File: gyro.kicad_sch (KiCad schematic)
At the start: 6 parts, among them U4 I3G4250D

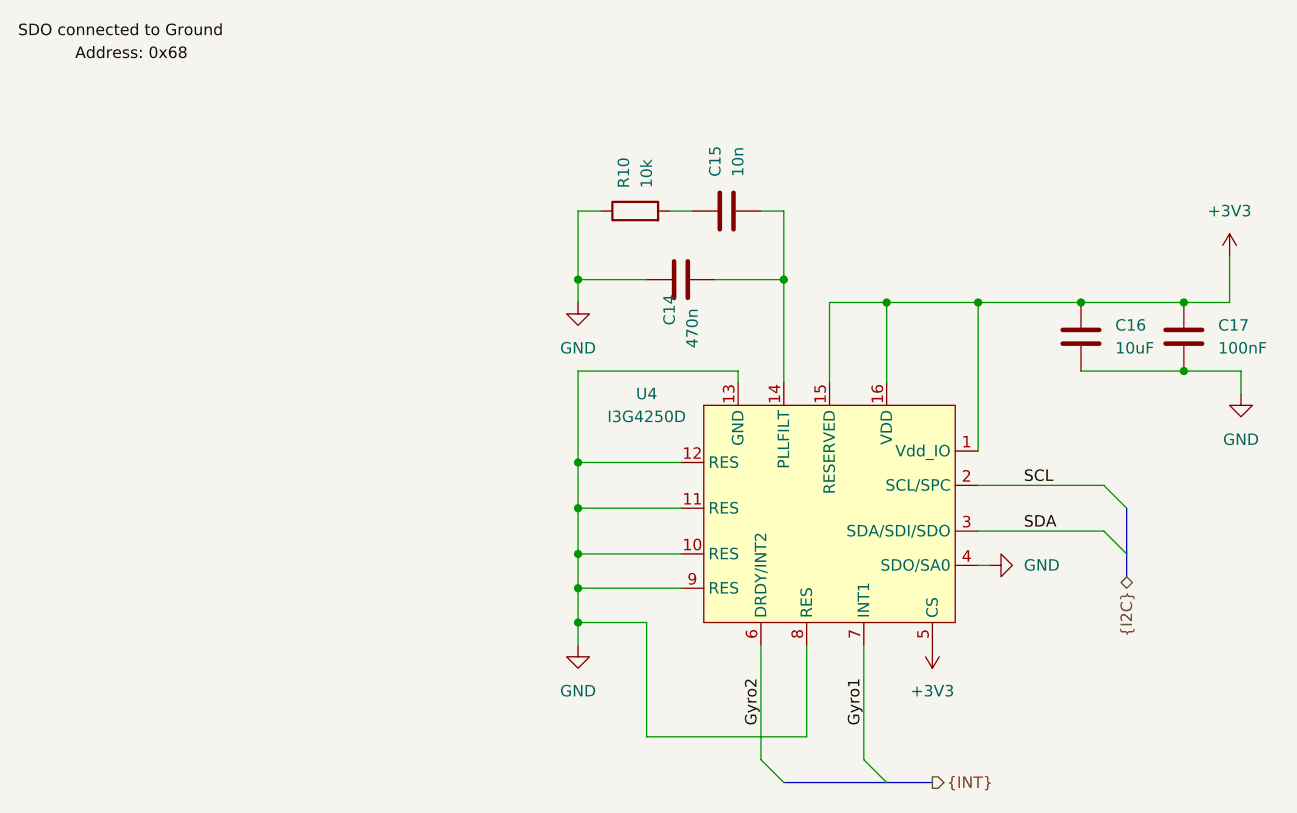
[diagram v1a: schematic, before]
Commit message: Geographical reannotated
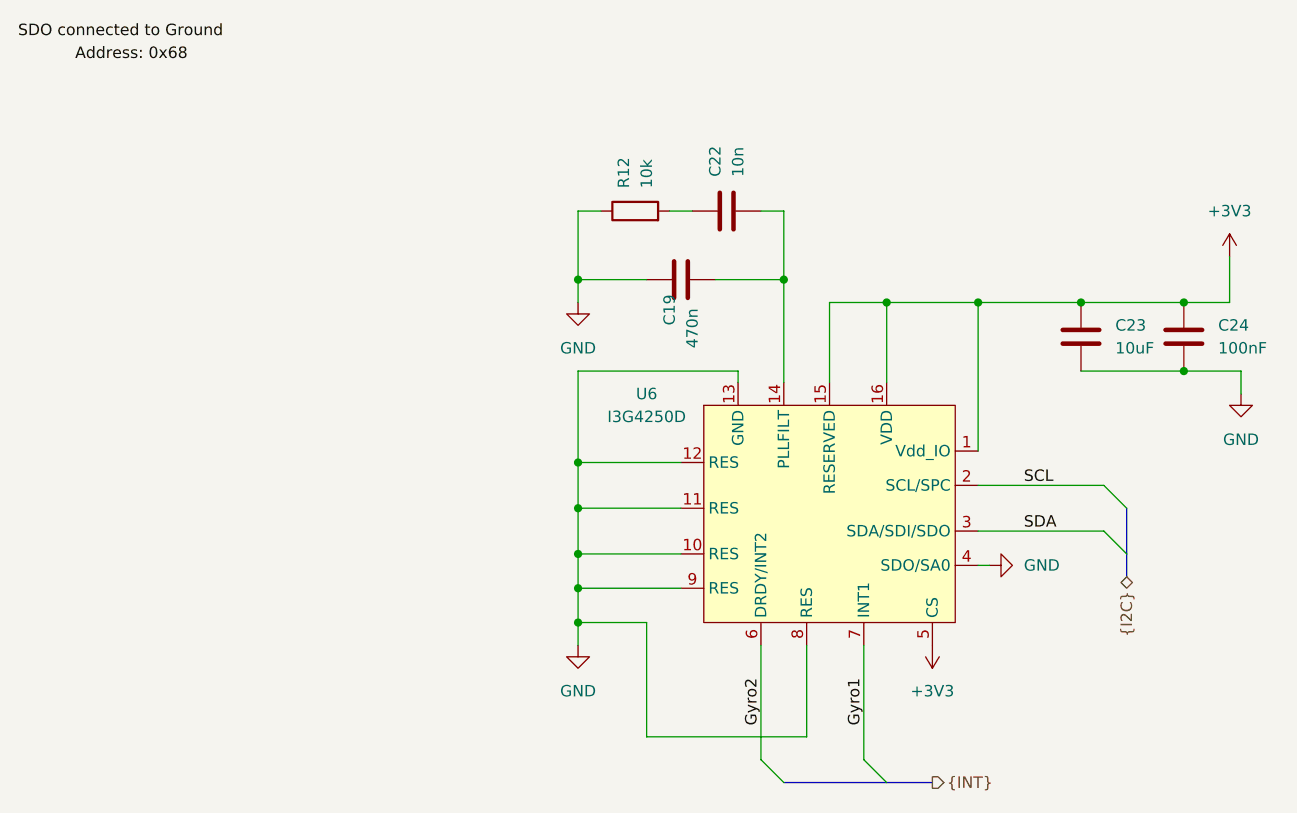
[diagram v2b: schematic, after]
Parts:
- renumbered C14 to C19, C15 to C22, C16 to C23, C17 to C24, R10 to R12, U4 to U6
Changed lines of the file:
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@@
   (symbol (lib_id "Device:C") (at 143.51 49.53 0) (unit 1)
     (in_bom yes) (on_board yes)
-    (property "Reference" "C17" (id 0) (at 147.32 48.26 0)
+    (property "Reference" "C24" (id 0) (at 147.32 48.26 0)
       (effects (font (size 1.27 1.27)) (justify left))
     )
@@
   (symbol (lib_id "Device:C") (at 132.08 49.53 0) (unit 1)
     (in_bom yes) (on_board yes)
-    (property "Reference" "C16" (id 0) (at 135.89 48.26 0)
+    (property "Reference" "C23" (id 0) (at 135.89 48.26 0)
       (effects (font (size 1.27 1.27)) (justify left))
     )
@@
   (symbol (lib_id "Device:C") (at 87.63 43.18 90) (mirror x) (unit 1)
     (in_bom yes) (on_board yes)
-    (property "Reference" "C14" (id 0) (at 86.36 48.26 0)
+    (property "Reference" "C19" (id 0) (at 86.36 48.26 0)
       (effects (font (size 1.27 1.27)) (justify right))
     )
@@
   (symbol (lib_id "Device:C") (at 92.71 35.56 270) (unit 1)
     (in_bom yes) (on_board yes) (fields_autoplaced)
-    (property "Reference" "C15" (id 0) (at 91.4399 31.75 0)
+    (property "Reference" "C22" (id 0) (at 91.4399 31.75 0)
       (effects (font (size 1.27 1.27)) (justify right))
     )
@@
   (symbol (lib_id "Device:R") (at 82.55 35.56 90) (unit 1)
     (in_bom yes) (on_board yes) (fields_autoplaced)
-    (property "Reference" "R10" (id 0) (at 81.2799 33.02 0)
+    (property "Reference" "R12" (id 0) (at 81.2799 33.02 0)
       (effects (font (size 1.27 1.27)) (justify left))
     )
@@
   (symbol (lib_id "Sensor:I3G4250D") (at 97.79 46.99 0) (unit 1)
     (in_bom yes) (on_board yes)
-    (property "Reference" "U4" (id 0) (at 83.82 55.88 0))
+    (property "Reference" "U6" (id 0) (at 83.82 55.88 0))
     (property "Value" "I3G4250D" (id 1) (at 83.82 58.42 0))
     (property "Footprint" "YAR_Sensors:I3G4250D" (id 2) (at 97.79 46.99 0)

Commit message: Final refinements before issue to JLC
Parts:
- renumbered C19 to C14, C22 to C15, C23 to C16, C24 to C17, R12 to R10, U6 to U4
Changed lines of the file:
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@@
   (symbol (lib_id "power:GND") (at 76.2 83.82 0) (unit 1)
     (in_bom yes) (on_board yes) (fields_autoplaced)
-    (property "Reference" "#PWR031" (id 0) (at 76.2 90.17 0)
+    (property "Reference" "#PWR033" (id 0) (at 76.2 90.17 0)
       (effects (font (size 1.27 1.27)) hide)
     )
@@
   (symbol (lib_id "Device:C") (at 143.51 49.53 0) (unit 1)
     (in_bom yes) (on_board yes)
-    (property "Reference" "C24" (id 0) (at 147.32 48.26 0)
+    (property "Reference" "C17" (id 0) (at 147.32 48.26 0)
       (effects (font (size 1.27 1.27)) (justify left))
     )
@@
   (symbol (lib_id "power:GND") (at 76.2 45.72 0) (unit 1)
     (in_bom yes) (on_board yes) (fields_autoplaced)
-    (property "Reference" "#PWR030" (id 0) (at 76.2 52.07 0)
+    (property "Reference" "#PWR032" (id 0) (at 76.2 52.07 0)
       (effects (font (size 1.27 1.27)) hide)
     )
@@
   (symbol (lib_id "Device:C") (at 132.08 49.53 0) (unit 1)
     (in_bom yes) (on_board yes)
-    (property "Reference" "C23" (id 0) (at 135.89 48.26 0)
+    (property "Reference" "C16" (id 0) (at 135.89 48.26 0)
       (effects (font (size 1.27 1.27)) (justify left))
     )
@@
   (symbol (lib_id "power:+3V3") (at 115.57 83.82 180) (unit 1)
     (in_bom yes) (on_board yes) (fields_autoplaced)
-    (property "Reference" "#PWR032" (id 0) (at 115.57 80.01 0)
+    (property "Reference" "#PWR034" (id 0) (at 115.57 80.01 0)
       (effects (font (size 1.27 1.27)) hide)
     )
@@
   (symbol (lib_id "power:+3V3") (at 148.59 40.64 0) (unit 1)
     (in_bom yes) (on_board yes) (fields_autoplaced)
-    (property "Reference" "#PWR034" (id 0) (at 148.59 44.45 0)
+    (property "Reference" "#PWR036" (id 0) (at 148.59 44.45 0)
       (effects (font (size 1.27 1.27)) hide)
     )
@@
   (symbol (lib_id "Device:C") (at 87.63 43.18 90) (mirror x) (unit 1)
     (in_bom yes) (on_board yes)
-    (property "Reference" "C19" (id 0) (at 86.36 48.26 0)
+    (property "Reference" "C14" (id 0) (at 86.36 48.26 0)
       (effects (font (size 1.27 1.27)) (justify right))
     )
@@
   (symbol (lib_id "power:GND") (at 149.86 55.88 0) (unit 1)
     (in_bom yes) (on_board yes) (fields_autoplaced)
-    (property "Reference" "#PWR035" (id 0) (at 149.86 62.23 0)
+    (property "Reference" "#PWR037" (id 0) (at 149.86 62.23 0)
       (effects (font (size 1.27 1.27)) hide)
     )
@@
   (symbol (lib_id "Device:C") (at 92.71 35.56 270) (unit 1)
     (in_bom yes) (on_board yes) (fields_autoplaced)
-    (property "Reference" "C22" (id 0) (at 91.4399 31.75 0)
+    (property "Reference" "C15" (id 0) (at 91.4399 31.75 0)
       (effects (font (size 1.27 1.27)) (justify right))
     )
@@
   (symbol (lib_id "Device:R") (at 82.55 35.56 90) (unit 1)
     (in_bom yes) (on_board yes) (fields_autoplaced)
-    (property "Reference" "R12" (id 0) (at 81.2799 33.02 0)
+    (property "Reference" "R10" (id 0) (at 81.2799 33.02 0)
       (effects (font (size 1.27 1.27)) (justify left))
     )
@@
   (symbol (lib_id "Sensor:I3G4250D") (at 97.79 46.99 0) (unit 1)
     (in_bom yes) (on_board yes)
-    (property "Reference" "U6" (id 0) (at 83.82 55.88 0))
+    (property "Reference" "U4" (id 0) (at 83.82 55.88 0))
     (property "Value" "I3G4250D" (id 1) (at 83.82 58.42 0))
     (property "Footprint" "YAR_Sensors:I3G4250D" (id 2) (at 97.79 46.99 0)
@@
   (symbol (lib_id "power:GND") (at 121.92 74.93 90) (unit 1)
     (in_bom yes) (on_board yes) (fields_autoplaced)
-    (property "Reference" "#PWR033" (id 0) (at 128.27 74.93 0)
+    (property "Reference" "#PWR035" (id 0) (at 128.27 74.93 0)
       (effects (font (size 1.27 1.27)) hide)
     )
